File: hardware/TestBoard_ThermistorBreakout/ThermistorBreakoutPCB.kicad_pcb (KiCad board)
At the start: 2 copper layers, 30 x 25 mm, 22 parts, among them J1 Conn_01x02, J3 Conn_01x03, J4 Conn_01x03, J5 Conn_01x03, J6 Conn_01x03, J8 Conn_01x06

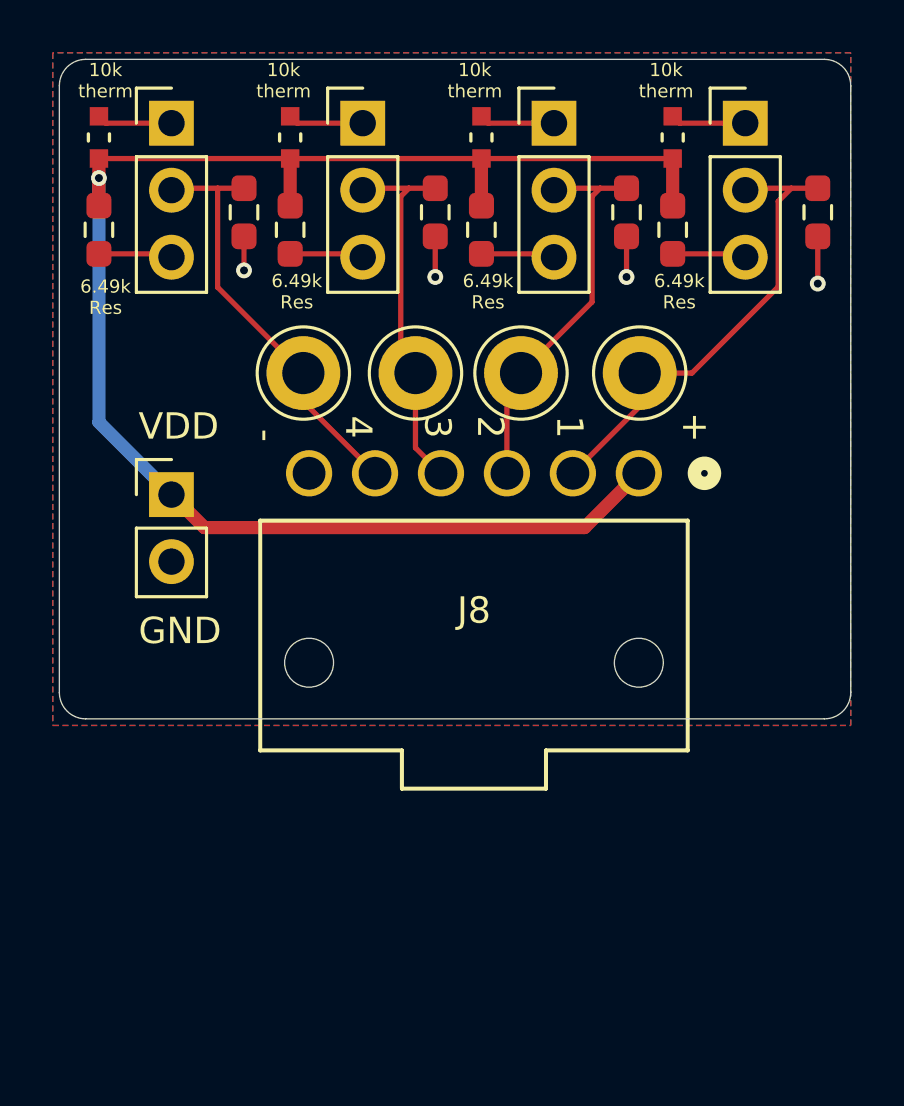
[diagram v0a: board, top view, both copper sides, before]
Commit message: Temperature Scrutineering PCB (#22)
* initial schematic and layout

* updated layout

* schematic with graphics/mounting

* graphics stuff

* fixed routing

* BOM and gerber (still need to find jack P/N)

* final

* revert back to main...

* added Scrutineering footprints

* added Scrutineering 3d models

* BOM and gerber with changed connector

* changed to vertical connectors

* added footprints/3d models vertical connectors

* fix 1 trace

* updated BOM

* updated BOM again

* Revert "fix 1 trace"

This reverts commit af0c854c5f9be3b18890f8714f235c97d2fe5d90.

:#

* Replaced Lakshay's tiny banana jacks with real ones

* fix unrouted

* Updated Gerbers

* Updated Thermistor Test Board

---------

Co-authored-by: Phoenix Nguyen <phoenixn831@gmail.com>
Co-authored-by: Ravi Shah <ravidhruvishshah@gmail.com>
Co-authored-by: kretsdyl <kretschmandk@gmail.com>
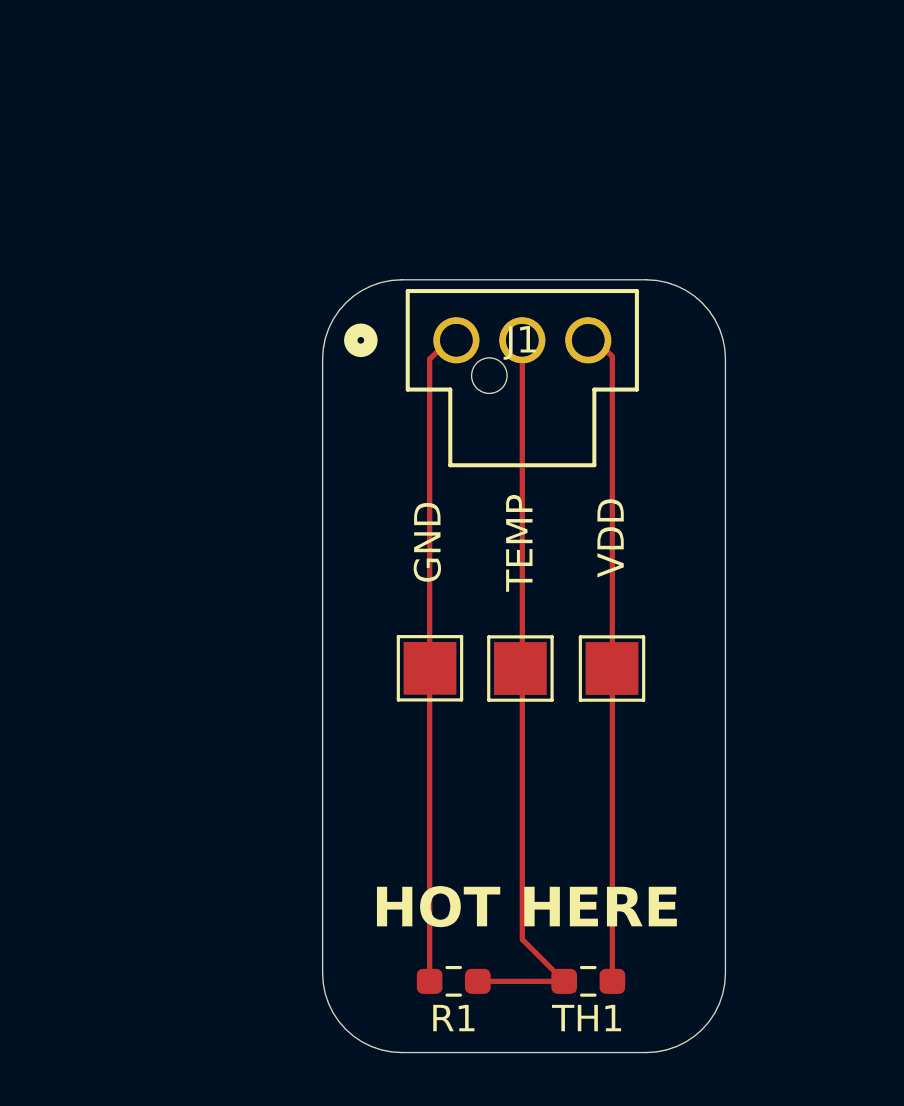
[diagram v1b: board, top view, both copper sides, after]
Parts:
- removed J3, J4, J5, J6: Conn_01x03, Connector_PinHeader_2.54mm:PinHeader_1x03_P2.54mm_Vertical
- removed J8: Conn_01x06, VoltTemp:1053131106
- removed R10, R11, R12, R5, R6, R7, R8, R9: 6.49k, Resistor_SMD:R_0603_1608Metric_Pad0.98x0.95mm_HandSolder
- removed TH5, TH6, TH7, TH8: Thermistor_NTC, UTSVT_Special:THERM_ERT-J1VR104FM
- removed TP10, TP11, TP8, TP9: TestPoint, TestPoint:TestPoint_Keystone_5005-5009_Compact
- added G***: LOGO, Images:hot, B.Cu at (122.9, 61.0)
- added R1: 6.49k, Resistor_SMD:R_0603_1608Metric_Pad0.98x0.95mm_HandSolder, F.Cu at (120.2, 72.7)
- added TH1: ERTJ1VR104FM, Resistor_SMD:R_0603_1608Metric_Pad0.98x0.95mm_HandSolder, F.Cu at (125.3, 72.7)
- added TP1: TestPoint, TestPoint:TestPoint_Pad_2.0x2.0mm, F.Cu at (119.3, 60.8)
- added TP2: TestPoint, TestPoint:TestPoint_Pad_2.0x2.0mm, F.Cu at (126.2, 60.8)
- added TP3: TestPoint, TestPoint:TestPoint_Pad_2.0x2.0mm, F.Cu at (122.7, 60.8)
- J1: value Conn_01x02 -> Conn_01x03; footprint Connector_PinHeader_2.54mm:PinHeader_1x02_P2.54mm_Vertical -> Scrutineering:CONN_SD-105309-100_03_MOL
- moved J1 12.3 mm to (120.3, 48.4)
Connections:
- J1 pad 1: VDDA -> /GND
- J1 pad 2: GNDA -> /TEMP
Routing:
- net VDDA: track 61.1 -> 0.00 mm, vias 1 -> 0
- net /TEMP: track 0.00 -> 28.2 mm
- net /GND: track 0.00 -> 24.9 mm
- net /VDD: track 0.00 -> 24.9 mm
- net /Temperature1: track 19.3 -> 0.00 mm
- net /Temperature2: track 16.2 -> 0.00 mm
- net /Temperature4: track 16.1 -> 0.00 mm
- net /Temperature3: track 14.3 -> 0.00 mm
- net GNDA: track 6.16 -> 0.00 mm, vias 4 -> 0
- net Net-(J3-Pin_1): track 2.86 -> 0.00 mm
- net Net-(J6-Pin_1): track 2.86 -> 0.00 mm
- net Net-(J5-Pin_1): track 2.86 -> 0.00 mm
- net Net-(J4-Pin_1): track 2.86 -> 0.00 mm
- net Net-(J6-Pin_3): track 2.80 -> 0.00 mm
- net Net-(J5-Pin_3): track 2.80 -> 0.00 mm
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- removed copper zone on B.Cu, net GNDA
- removed copper zone on F.Cu, net GNDA
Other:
- board size 30 x 25 mm -> 15.3 x 29.3 mm
- board text added: "HOT HERE"
- board text added: "TEMP"
- board text removed: "+"
- board text removed: "-"
- board text removed: "1"
- board text removed: "10k therm"
- board text removed: "2"
- board text removed: "3"
- board text removed: "4"
- board text removed: "6.49k Res"
